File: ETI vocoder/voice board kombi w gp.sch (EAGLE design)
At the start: 174 parts, among them IC1 TL072P, IC1. TL072P, IC2 TL072P, IC2. TL072P, IC3 TL081P, IC3. TL081P, IC4 TL081P, IC4. TL081P, IC5 TL072P, IC6 LM13600AN, IC7 TL072P, IC7. TL072P, P1 C-OR-R050_075-025X100, P1. C-OR-R050_075-025X100, P10 C-OR-R050_075-025X100, P10. C-OR-R050_075-025X100, P11 C-OR-R050_075-025X100, P11. C-OR-R050_075-025X100, P12 C-OR-R050_075-025X100, P12. C-OR-R050_075-025X100, P13 C-OR-R050_075-025X100, P13. C-OR-R050_075-025X100, P14 C-OR-R050_075-025X100, P14. C-OR-R050_075-025X100, P15 C-OR-R050_075-025X100, P15. C-OR-R050_075-025X100, P16 C-OR-R050_075-025X100, P16. C-OR-R050_075-025X100, P2 C-OR-R050_075-025X100, P2. C-OR-R050_075-025X100, P3 C-OR-R050_075-025X100, P3. C-OR-R050_075-025X100, P4 C-OR-R050_075-025X100, P4. C-OR-R050_075-025X100, P5 C-OR-R050_075-025X100, P5. C-OR-R050_075-025X100, P6 C-OR-R050_075-025X100, P6. C-OR-R050_075-025X100, P7 C-OR-R050_075-025X100, P7. C-OR-R050_075-025X100, P8 C-OR-R050_075-025X100, P8. C-OR-R050_075-025X100, P9 C-OR-R050_075-025X100, P9. C-OR-R050_075-025X100, Q1 BF244C, Q1. BF244C, Q2 BC212L, Q2. BC212L

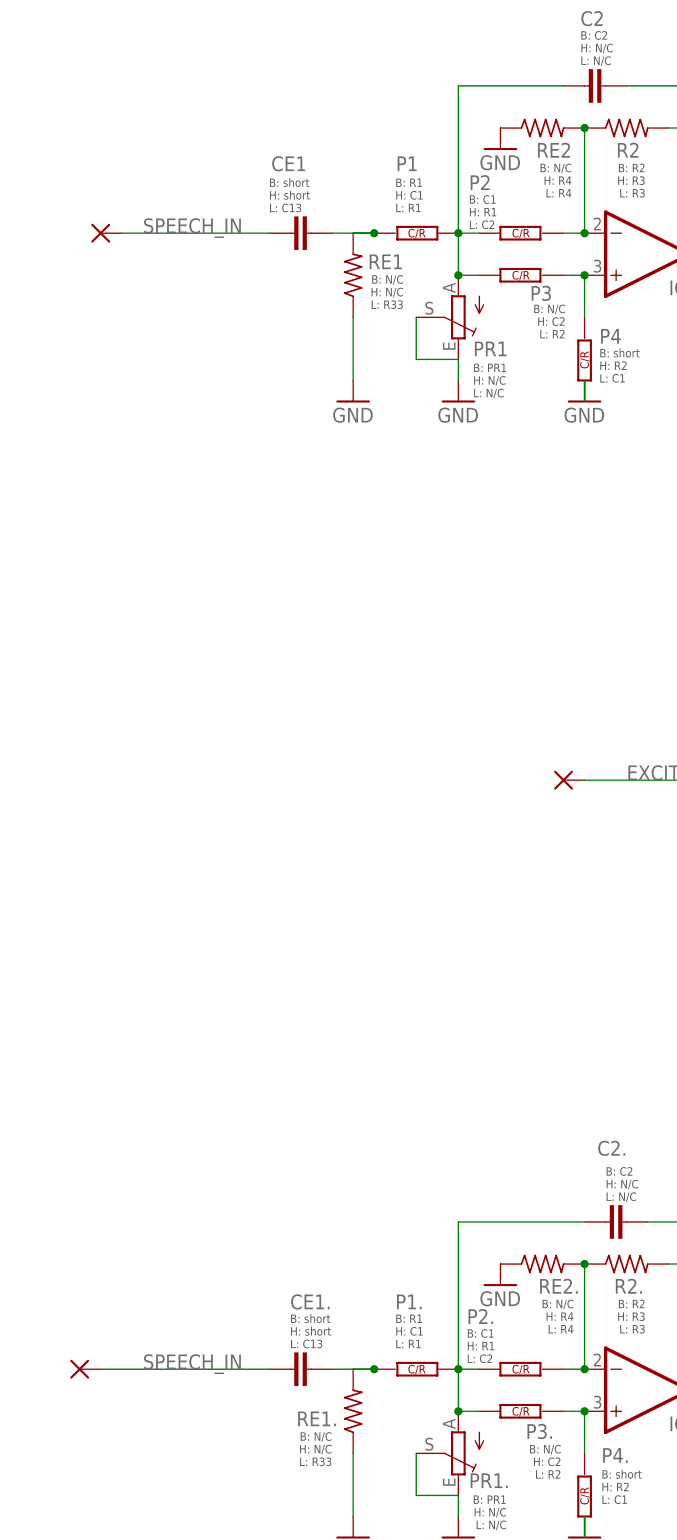
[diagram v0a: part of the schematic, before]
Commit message: Send combined 4 to production. Fixed wrong CE1 footprint for voice cards. Removed outline from combined 4 that covered too much of a slot
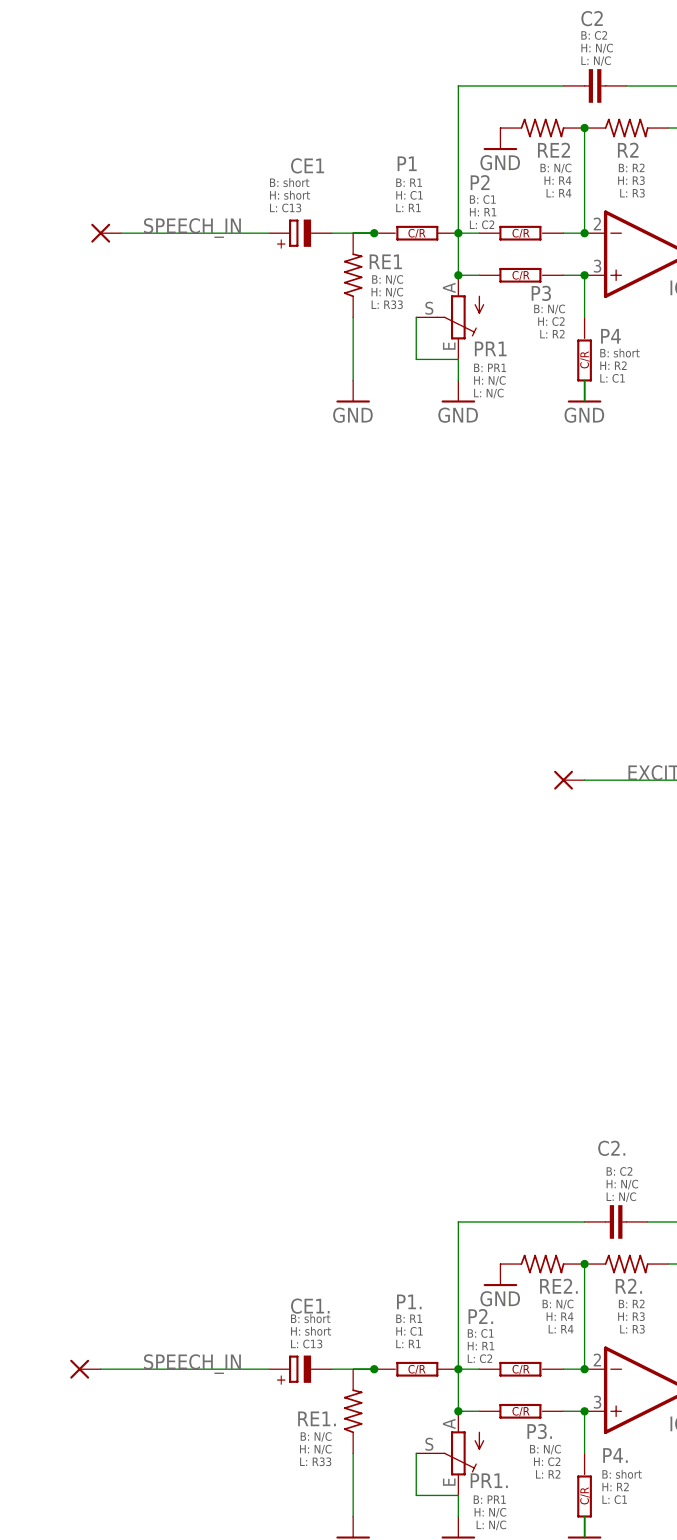
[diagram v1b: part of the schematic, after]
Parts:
- CE1, CE1.: device joakim:C-EU050_075-025X100 -> resistor:CPOL-EUE2-4
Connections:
- net N$43: now also CE1.-; no longer CE1.1
- net N$88: now also CE1..-; no longer CE1..1
- net SPEECH_IN: now also CE1.+, CE1..+; no longer CE1..2, CE1.2
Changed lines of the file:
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@@
 <part name="IC3" library="linear" deviceset="TL081" device="P"/>
 <part name="IC4" library="linear" deviceset="TL081" device="P"/>
-<part name="CE1" library="joakim" deviceset="C-EU" device="050_075-025X100"/>
 <part name="RE2" library="resistor" deviceset="R-US_" device="0207/7"/>
 <part name="GND17" library="supply1" deviceset="GND" device=""/>
@@
 <part name="IC3." library="linear" deviceset="TL081" device="P"/>
 <part name="IC4." library="linear" deviceset="TL081" device="P"/>
-<part name="CE1." library="joakim" deviceset="C-EU" device="050_075-025X100"/>
 <part name="RE2." library="resistor" deviceset="R-US_" device="0207/7"/>
 <part name="GND39" library="supply1" deviceset="GND" device=""/>
@@
 <part name="PAD18" library="wirepad" deviceset="WIREPAD" device="2,54/1,1"/>
 <part name="JP1" library="jumper" deviceset="JP1E" device=""/>
+<part name="CE1" library="resistor" deviceset="CPOL-EU" device="E2-4"/>
+<part name="CE1." library="resistor" deviceset="CPOL-EU" device="E2-4"/>
 </parts>
 <sheets>
@@
 </instance>
 <instance part="IC4" gate="A" x="243.84" y="195.58"/>
-<instance part="CE1" gate="G$1" x="2.54" y="205.74" smashed="yes" rot="R270">
-<attribute name="NAME" x="2.032" y="215.011" size="1.778" layer="95" rot="R180"/>
-<attribute name="VALUE" x="-2.159" y="204.216" size="1.778" layer="96" rot="R270"/>
-</instance>
 <instance part="RE2" gate="G$1" x="30.48" y="218.44" smashed="yes">
 <attribute name="NAME" x="29.718" y="214.8586" size="1.778" layer="95"/>
@@
 </instance>
 <instance part="IC4." gate="A" x="243.84" y="58.42"/>
-<instance part="CE1." gate="G$1" x="2.54" y="68.58" smashed="yes" rot="R270">
-<attribute name="NAME" x="0" y="75.819" size="1.778" layer="95"/>
-<attribute name="VALUE" x="-2.159" y="67.056" size="1.778" layer="96" rot="R270"/>
-</instance>
 <instance part="RE2." gate="G$1" x="30.48" y="81.28" smashed="yes">
 <attribute name="NAME" x="29.972" y="77.6986" size="1.778" layer="95"/>
@@
 <instance part="PAD18" gate="G$1" x="309.88" y="2.54" smashed="yes"/>
 <instance part="JP1" gate="A" x="205.74" y="246.38"/>
+<instance part="CE1" gate="G$1" x="0" y="205.74" smashed="yes" rot="R90">
+<attribute name="NAME" x="0" y="212.979" size="1.778" layer="95"/>
+<attribute name="VALUE" x="4.699" y="207.264" size="1.778" layer="96" rot="R90"/>
+</instance>
+<instance part="CE1." gate="G$1" x="0" y="68.58" smashed="yes" rot="R90">
+<attribute name="NAME" x="0" y="75.311" size="1.778" layer="95"/>
+<attribute name="VALUE" x="4.699" y="70.104" size="1.778" layer="96" rot="R90"/>
+</instance>
 </instances>
 <busses>
@@
 <label x="-17.78" y="68.58" size="1.778" layer="95"/>
 <wire x1="-2.54" y1="68.58" x2="-22.86" y2="68.58" width="0.1524" layer="91"/>
-<pinref part="CE1." gate="G$1" pin="2"/>
-</segment>
-<segment>
-<pinref part="CE1" gate="G$1" pin="2"/>
+<pinref part="CE1." gate="G$1" pin="+"/>
+</segment>
+<segment>
 <pinref part="PAD6" gate="G$1" pin="P"/>
 <wire x1="-20.32" y1="205.74" x2="-2.54" y2="205.74" width="0.1524" layer="91"/>
 <label x="-17.78" y="205.74" size="1.778" layer="95"/>
+<pinref part="CE1" gate="G$1" pin="+"/>
 </segment>
 </net>
@@
 <segment>
 <pinref part="RE1" gate="G$1" pin="2"/>
-<pinref part="CE1" gate="G$1" pin="1"/>
 <wire x1="5.08" y1="205.74" x2="10.16" y2="205.74" width="0.1524" layer="91"/>
 <pinref part="P1" gate="G$1" pin="2"/>
 <junction x="10.16" y="205.74"/>
 <wire x1="10.16" y1="205.74" x2="7.62" y2="205.74" width="0.1524" layer="91"/>
+<pinref part="CE1" gate="G$1" pin="-"/>
 </segment>
 </net>
@@
 <segment>
 <pinref part="RE1." gate="G$1" pin="2"/>
-<pinref part="CE1." gate="G$1" pin="1"/>
 <wire x1="5.08" y1="68.58" x2="10.16" y2="68.58" width="0.1524" layer="91"/>
 <pinref part="P1." gate="G$1" pin="2"/>
 <junction x="10.16" y="68.58"/>
 <wire x1="10.16" y1="68.58" x2="7.62" y2="68.58" width="0.1524" layer="91"/>
-</segment>
-</net>
+<pinref part="CE1." gate="G$1" pin="-"/>
+</segment>
+</net>
